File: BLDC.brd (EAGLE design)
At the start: 45.7 x 83.8 mm, 137 parts, among them U1 MCP2562, U2 STM32F405RGT6, U3 LM3671MF-3.3/NOPB, U4 DRV8302, Y1 8MHz

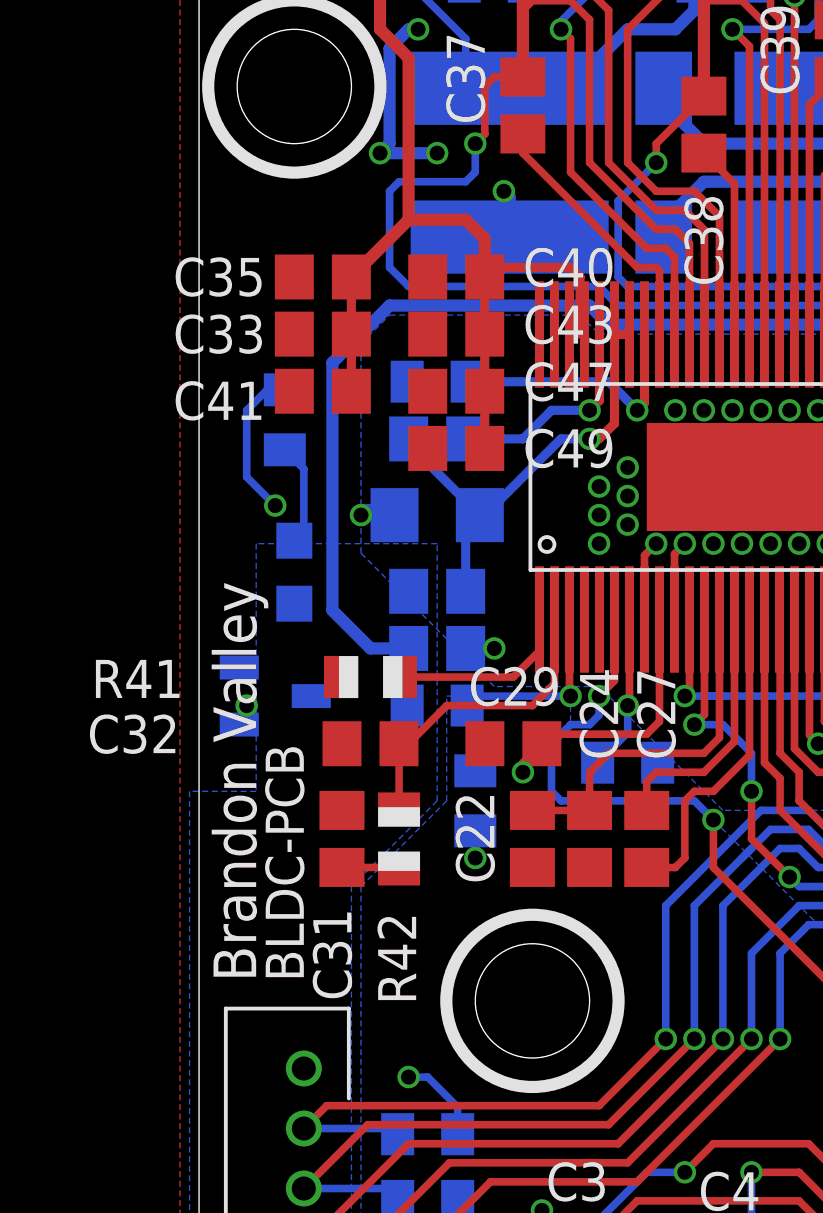
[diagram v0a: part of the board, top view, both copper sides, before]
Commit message: added big inductor and updated BOM a bit
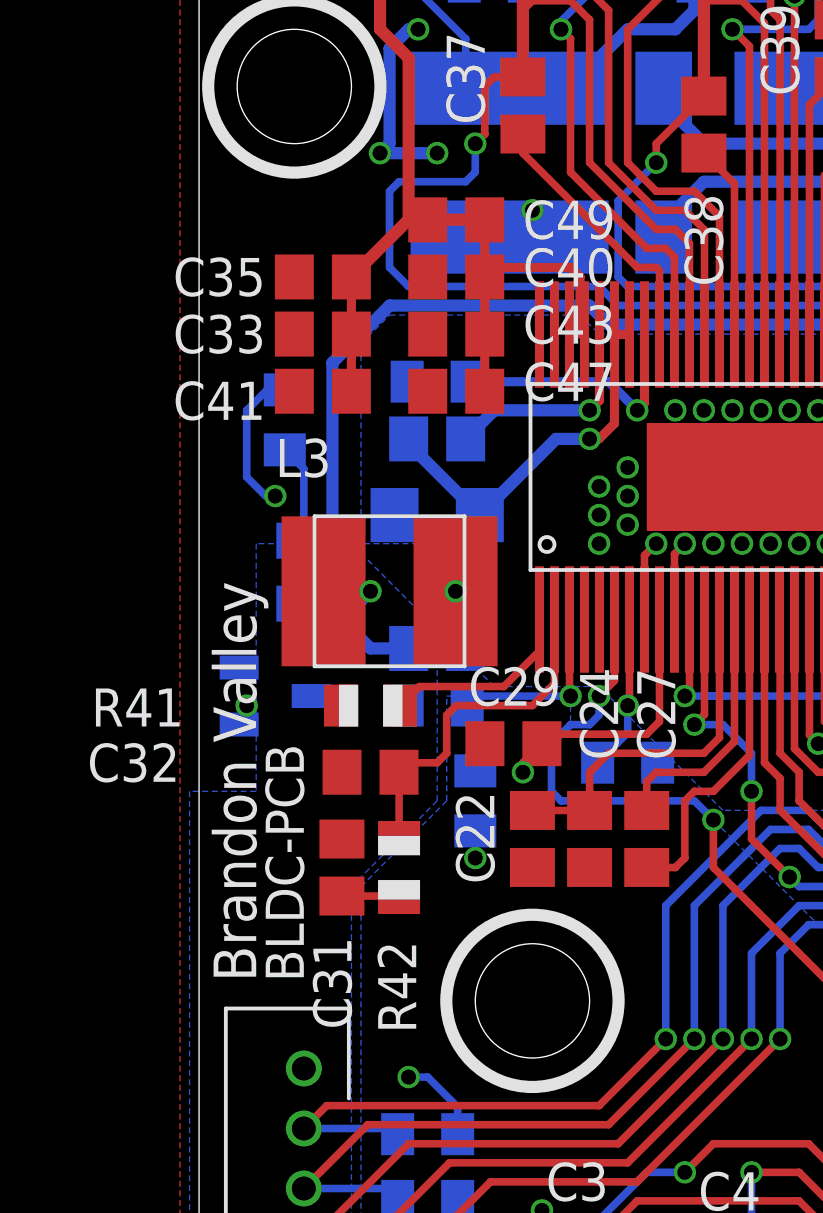
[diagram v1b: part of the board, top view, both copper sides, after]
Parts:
- removed L2: 22uH, FormE:0805
- added L3: 22uH, FormE:TYS5040220M-10
- C40: value 10uf, 50V -> 10uf,50V
- moved C49 7.62 mm to (8.57, 49.8)
- moved C31 0.95 mm to (4.76, 28.3)
- moved R41 0.95 mm to (5.71, 33.7)
- moved R42 0.95 mm to (6.67, 28.3)
- moved C32 0.95 mm to (5.71, 31.4)
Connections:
- net +5V: now also L3.P$2; no longer L2.2
- net N$21: now also L3.P$1; no longer L2.1
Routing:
- net +5V: track 103.1 -> 106.2 mm, vias 4 -> 5
- net GND: track 94.7 -> 91.9 mm, vias 76 -> 74
- net VCC: track 74.9 -> 72.7 mm
- net N$12: track 10.3 -> 11.8 mm
- net N$21: track 15.5 -> 16.6 mm, vias 1 -> 2

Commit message: added some large components at the last minute because I am a glutton for punishment
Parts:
- removed C33: 10uf,50V, rcl:C0805
- removed C44: 100n, rcl:C0805
- added C50: 10uf,50V, rcl:C1206
- added C51: 15uf,100V, FormE:K-55
- C34, C35, C36, C40, C42: device rcl:C0805 -> rcl:C1206
- C41: value 15uf,100V -> 10uf,50V; device rcl:C0805 -> rcl:C1206
- C43: value 10uf,50V -> 15uf,100V; device rcl:C0805 -> FormE:K-55
- C45: value 2.2n -> 100n
- C47: value 10uf,50V -> 2.2n
- C48: value 100uf -> 10uf,50V; device rcl:C0805 -> rcl:C1206
- C49: value 15uf,100V -> 100uf
- moved C45 26.4 mm to (10.2, 42.5), turned to 0 degrees
- moved C47 25.6 mm to (33.0, 51.8), flipped to the bottom, turned to 270 degrees
- moved C49 14.3 mm to (7.94, 35.6), flipped to the bottom
- moved C48 8.13 mm to (2.86, 41.9), turned to 0 degrees
- moved C43 7.63 mm to (3.17, 51.4), flipped to the bottom, turned to 90 degrees
- moved C40 7.38 mm to (1.91, 51.1), turned to 90 degrees
- moved C34 6.63 mm to (29.5, 51.8), turned to 270 degrees
- moved R53 5.93 mm to (9.84, 57.5)
- moved R30 5.32 mm to (1.27, 38.1)
- moved C42 4.97 mm to (27.0, 46.7)
- moved D2 3.31 mm to (11.1, 39.1), turned to 270 degrees
- moved C35 3.19 mm to (4.45, 51.1), turned to 90 degrees
- moved R43 2.22 mm to (10.2, 44.5)
- moved C41 2.03 mm to (2.86, 45.7), flipped to the bottom, turned to 0 degrees
- moved R51 1.91 mm to (9.84, 59.7)
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- renumbered L3 to L2
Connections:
- net +5V: now also C49.1; no longer C48.1
- net GND: now also C50.2, C51.2; no longer C33.2, C47.2
- net N$20: now also C45.1; no longer C44.1
- net N$21: now also C45.2; no longer C44.2
- net N$24: now also C46.1; no longer C45.1
- net N$26: now also C46.2; no longer C45.2
- net N$28: now also C47.2; no longer C46.2
- net N$29: now also C47.1; no longer C46.1
- net VCC: now also C48.1, C50.1, C51.1; no longer C33.1, C47.1, C49.1
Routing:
- net VCC: track 72.7 -> 81.6 mm, vias 0 -> 1
- net GND: track 91.9 -> 100.2 mm, vias 74 -> 77
- net N$24: track 22.6 -> 27.6 mm
- net H1_LOW: track 40.4 -> 35.7 mm
- net N$29: track 17.0 -> 20.2 mm
- net N$33: track 9.75 -> 6.65 mm
- net N$28: track 17.1 -> 19.7 mm
- net N$22: track 8.69 -> 6.47 mm
- net N$20: track 7.19 -> 4.97 mm
- net M_L1: track 16.2 -> 17.6 mm
- net N$21: track 16.6 -> 15.2 mm
- net ADC_TEMP: track 57.4 -> 56.2 mm
- net H3_VS: track 57.2 -> 58.1 mm
- net M_L3: track 21.4 -> 22.1 mm
- net +5V: track 106.2 -> 106.8 mm
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
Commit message: updated BOM
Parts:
- removed C50: 10uf,50V, rcl:C1206
- removed C51: 15uf,100V, FormE:K-55
- added C33: 15uf,100V, FormE:K-55
- added C44: 100n, rcl:C0805
- C45: value 100n -> 2.2n
- C47: value 2.2n -> 10uf,50V; device rcl:C0805 -> rcl:C1206
- C48: value 10uf,50V -> 100uf; device rcl:C1206 -> rcl:C0805
- C49: value 100uf -> 10uf,50V; device rcl:C0805 -> rcl:C1206
- moved R2 32.6 mm to (-7.30, -10.5)
- moved C47 31.7 mm to (2.86, 41.9), turned to 0 degrees
- moved C45 26.4 mm to (34.9, 51.8), turned to 270 degrees
- moved C49 9.69 mm to (2.86, 43.8), turned to 0 degrees
- moved C48 8.13 mm to (7.94, 35.6), turned to 180 degrees
- moved C43 8.11 mm to (7.30, 44.5), flipped to the top, turned to 270 degrees
- moved C46 1.90 mm to (33.0, 51.8)
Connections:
- net +5V: now also C48.1, R2.2; no longer C49.1, R2.1
- net GND: now also C33.2, C47.2; no longer C50.2, C51.2
- net N$20: now also C44.1; no longer C45.1
- net N$21: now also C44.2; no longer C45.2
- net N$24: now also C45.1; no longer C46.1
- net N$26: now also C45.2; no longer C46.2
- net N$28: now also C46.2; no longer C47.2
- net N$29: now also C46.1; no longer C47.1
- net N$5: now also R2.1; no longer R2.2
- net VCC: now also C33.1, C47.1, C49.1; no longer C48.1, C50.1, C51.1
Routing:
- net N$5: track 5.68 -> 4.40 mm
- net +5V: track 106.8 -> 105.9 mm

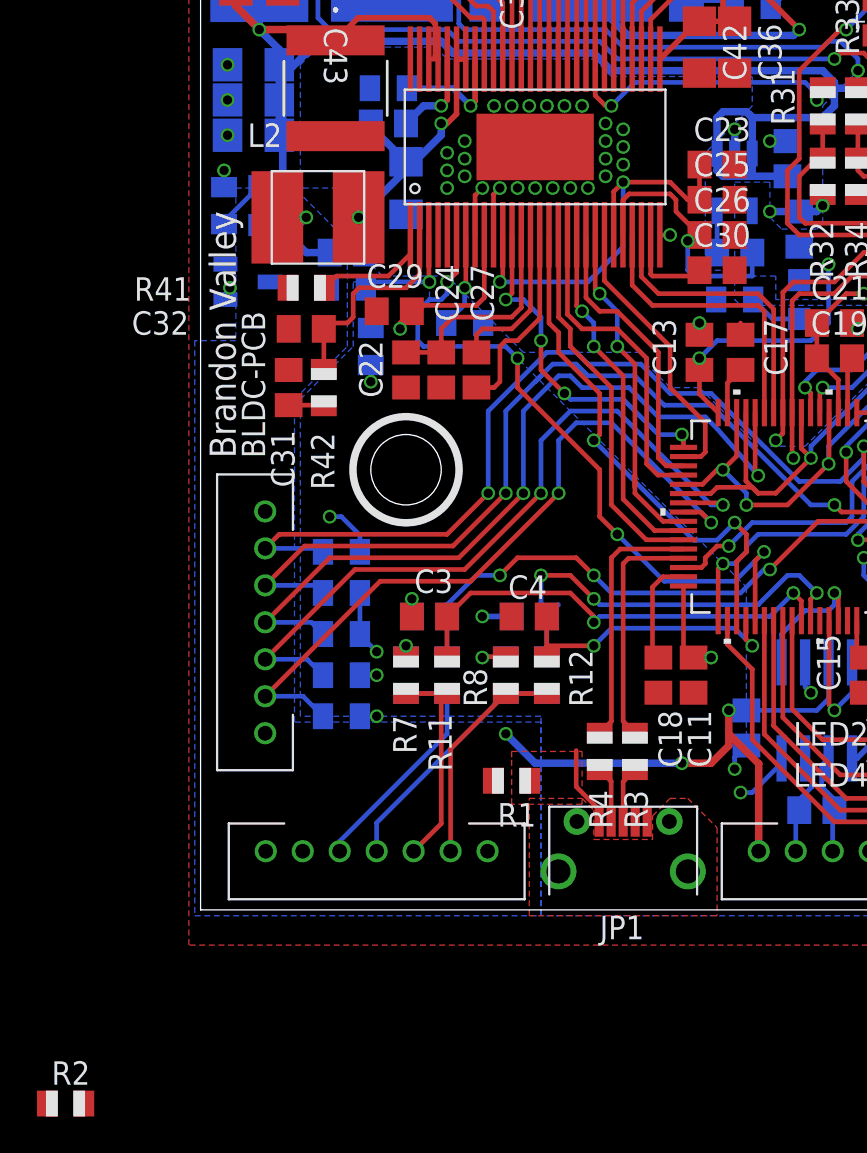
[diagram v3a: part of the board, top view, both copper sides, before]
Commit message: added jumper for DNP on usb
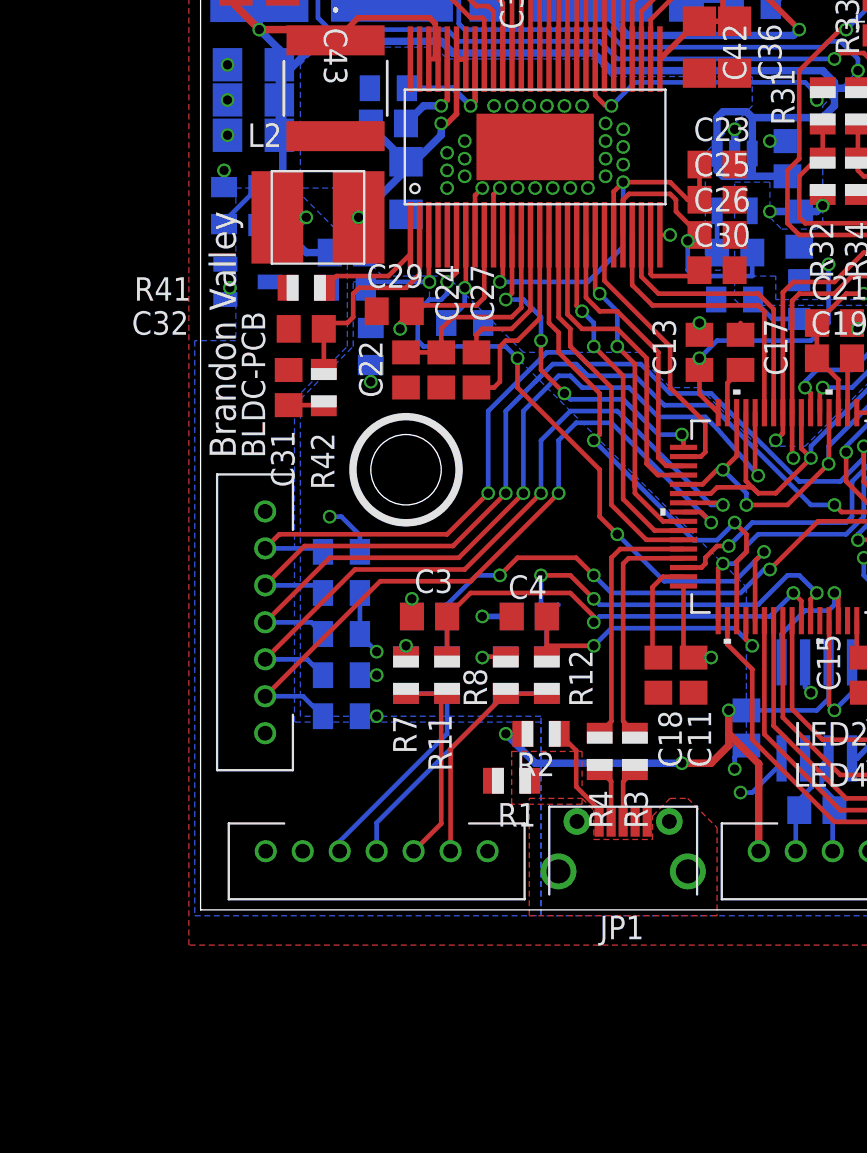
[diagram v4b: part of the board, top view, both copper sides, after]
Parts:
- moved R2 32.6 mm to (18.4, 9.53), turned to 180 degrees
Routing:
- net N$5: track 4.40 -> 5.68 mm
- net +5V: track 105.9 -> 106.6 mm
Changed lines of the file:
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@@
 <attribute name="PARTNO" value="KCM55WR72A156MH01K" x="7.3025" y="44.45" size="1.778" layer="27" rot="R270" display="off"/>
 </element>
-<element name="R2" library="adafruit" package="R0805" value="DNP" x="-7.3025" y="-10.4775">
-<attribute name="PARTNO" value="ERJ-6GEY0R00V" x="-7.3025" y="-10.4775" size="1.4224" layer="27" display="off"/>
+<element name="R2" library="adafruit" package="R0805" value="DNP" x="18.415" y="9.525" rot="R180">
+<attribute name="PARTNO" value="ERJ-6GEY0R00V" x="18.415" y="9.525" size="1.4224" layer="27" rot="R180" display="off"/>
 </element>
 </elements>
@@
 <wire x1="27.6225" y1="7.9375" x2="28.575" y2="8.89" width="0.4064" layer="1"/>
 <wire x1="28.575" y1="8.89" x2="28.575" y2="9.525" width="0.4064" layer="1"/>
-<wire x1="29.68625" y1="43.02125" x2="29.845" y2="42.8625" width="0.4064" layer="16"/>
 <wire x1="29.68625" y1="43.02125" x2="29.5275" y2="43.18" width="0.4064" layer="16"/>
 <wire x1="29.5275" y1="43.18" x2="28.2575" y2="43.18" width="0.4064" layer="16"/>
@@
 <wire x1="34.29" y1="43.4975" x2="33.655" y2="42.8625" width="0.4064" layer="16"/>
 <contactref element="R2" pad="2"/>
-<wire x1="5.525" y1="3.175" x2="-6.3025" y2="-10.4775" width="0" layer="19" extent="1-1"/>
+<wire x1="17.415" y1="9.525" x2="16.51" y2="9.525" width="0.254" layer="1"/>
 </signal>
 <signal name="+3V3">
@@
 <wire x1="21.56" y1="4.7578" x2="21.59" y2="4.7878" width="0.254" layer="1"/>
 <wire x1="21.59" y1="4.7878" x2="21.59" y2="5.3975" width="0.254" layer="1"/>
-<wire x1="20.32" y1="6.6675" x2="20.32" y2="8.62" width="0.254" layer="1"/>
+<wire x1="20.32" y1="8.62" x2="20.32" y2="6.6675" width="0.254" layer="1"/>
 <wire x1="21.59" y1="5.3975" x2="20.32" y2="6.6675" width="0.254" layer="1"/>
 <contactref element="R2" pad="1"/>
-<wire x1="-8.3025" y1="-10.4775" x2="20.32" y2="6.6675" width="0" layer="19" extent="1-1"/>
+<wire x1="19.415" y1="9.525" x2="20.32" y2="8.62" width="0.254" layer="1"/>
 </signal>
 <signal name="N$3">

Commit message: fixed brd errors
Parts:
- moved C20 0.71 mm to (32.4, 41.0)
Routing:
- net N$24: track 27.6 -> 28.8 mm
- net +5V: track 106.6 -> 106.0 mm
- net GND: track 100.2 -> 100.0 mm, vias 77 -> 76
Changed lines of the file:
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@@
 <attribute name="VALUE" x="39.37" y="19.3675" size="1.27" layer="28" rot="MR0"/>
 </element>
-<element name="C20" library="rcl" package="C0805" value="4.7uF" x="31.75" y="40.64" smashed="yes" rot="MR90">
-<attribute name="PARTNO" value="GRM21BC81E475KA12L" x="31.75" y="40.64" size="1.778" layer="28" rot="MR90" display="off"/>
-<attribute name="NAME" x="33.02" y="39.37" size="1.27" layer="26" rot="MR90"/>
-<attribute name="VALUE" x="29.21" y="39.37" size="1.27" layer="28" rot="MR90"/>
+<element name="C20" library="rcl" package="C0805" value="4.7uF" x="32.385" y="40.9575" smashed="yes" rot="MR90">
+<attribute name="PARTNO" value="GRM21BC81E475KA12L" x="32.385" y="40.9575" size="1.778" layer="28" rot="MR90" display="off"/>
+<attribute name="NAME" x="33.655" y="39.6875" size="1.27" layer="26" rot="MR90"/>
+<attribute name="VALUE" x="29.845" y="39.6875" size="1.27" layer="28" rot="MR90"/>
 </element>
 <element name="C8" library="rcl" package="C0805" value="15p" x="38.1" y="16.8275" smashed="yes" rot="MR0">
@@
 <vertex x="21.2725" y="46.0375"/>
 <vertex x="22.225" y="45.085"/>
-<vertex x="29.845" y="45.085"/>
-<vertex x="29.845" y="43.4975"/>
-<vertex x="27.305" y="40.9575"/>
+<vertex x="33.9725" y="45.085"/>
+<vertex x="33.9725" y="40.3225"/>
+<vertex x="27.305" y="40.3225"/>
 <vertex x="27.305" y="34.6075"/>
 <vertex x="28.8925" y="34.6075"/>
@@
 <wire x1="28.8925" y1="40.92" x2="28.8925" y2="42.2275" width="0.4064" layer="16"/>
 <via x="28.8925" y="42.2275" extent="1-16" drill="0.5"/>
-<wire x1="31.75" y1="41.59" x2="31.7475" y2="41.5925" width="0.254" layer="16"/>
 <wire x1="32.385" y1="37.78" x2="30.8" y2="37.78" width="0.4064" layer="16"/>
 <wire x1="30.8" y1="37.78" x2="30.7975" y2="37.7825" width="0.4064" layer="16"/>
 <via x="30.7975" y="37.7825" extent="1-16" drill="0.5"/>
-<wire x1="31.7475" y1="41.5925" x2="30.7975" y2="41.5925" width="0.4064" layer="16"/>
-<via x="30.7975" y="41.5925" extent="1-16" drill="0.5"/>
 <wire x1="33.655" y1="38.6875" x2="33.655" y2="38.1" width="0.4064" layer="1"/>
 <via x="33.655" y="38.1" extent="1-16" drill="0.5"/>
@@
 <contactref element="C14" pad="2"/>
 <contactref element="C21" pad="2"/>
-<wire x1="10.3525" y1="49.2725" x2="11.1125" y2="50.0325" width="0.254" layer="16"/>
-<wire x1="11.1125" y1="50.0325" x2="11.1125" y2="50.165" width="0.254" layer="16"/>
-<via x="11.1125" y="50.165" extent="1-16" drill="0.5"/>
+<via x="10.16" y="51.1175" extent="1-16" drill="0.5"/>
 <contactref element="C35" pad="2"/>
 <contactref element="C40" pad="2"/>
@@
 <via x="1.4575" y="43.815" extent="1-16" drill="0.5"/>
 <via x="1.4575" y="45.72" extent="1-16" drill="0.5"/>
+<wire x1="10.16" y1="51.1175" x2="10.3525" y2="50.925" width="0.4064" layer="16"/>
+<wire x1="10.3525" y1="50.925" x2="10.3525" y2="49.2725" width="0.4064" layer="16"/>
 </signal>
 <signal name="+5V">
@@
 <wire x1="27.6225" y1="7.9375" x2="28.575" y2="8.89" width="0.4064" layer="1"/>
 <wire x1="28.575" y1="8.89" x2="28.575" y2="9.525" width="0.4064" layer="1"/>
-<wire x1="29.68625" y1="43.02125" x2="29.5275" y2="43.18" width="0.4064" layer="16"/>
 <wire x1="29.5275" y1="43.18" x2="28.2575" y2="43.18" width="0.4064" layer="16"/>
 <wire x1="28.2575" y1="43.18" x2="27.94" y2="42.8625" width="0.4064" layer="16"/>
@@
 <wire x1="18.0975" y1="7.9375" x2="16.51" y2="9.525" width="0.4064" layer="16"/>
 <wire x1="26.035" y1="7.9375" x2="18.0975" y2="7.9375" width="0.4064" layer="16"/>
-<wire x1="4.445" y1="45.085" x2="6.35" y2="46.99" width="0.4064" layer="16"/>
 <contactref element="LED5" pad="A"/>
 <wire x1="5.715" y1="35.56" x2="4.445" y2="36.83" width="0.4064" layer="16"/>
-<wire x1="4.445" y1="36.83" x2="4.445" y2="45.085" width="0.4064" layer="16"/>
 <contactref element="L2" pad="P$2"/>
 <wire x1="4.445" y1="36.83" x2="5.08" y2="36.83" width="0.4064" layer="16"/>
-<wire x1="5.08" y1="36.83" x2="5.715" y2="37.465" width="0.4064" layer="16"/>
+<wire x1="5.715" y1="37.465" x2="5.08" y2="36.83" width="0.4064" layer="16"/>
 <via x="5.715" y="37.465" extent="1-16" drill="0.5"/>
 <wire x1="5.715" y1="37.465" x2="4.15" y2="37.465" width="0.4064" layer="1"/>
 <wire x1="34.29" y1="44.7675" x2="34.29" y2="44.45" width="0.4064" layer="16"/>
-<wire x1="31.75" y1="39.69" x2="29.2125" y2="39.69" width="0.4064" layer="16"/>
 <wire x1="29.2125" y1="39.69" x2="29.21" y2="39.6875" width="0.4064" layer="16"/>
-<wire x1="34.29" y1="44.45" x2="34.29" y2="43.4975" width="0.4064" layer="16"/>
-<wire x1="33.655" y1="42.8625" x2="29.845" y2="42.8625" width="0.4064" layer="16"/>
-<wire x1="29.845" y1="42.8625" x2="29.68625" y2="43.02125" width="0.4064" layer="16"/>
-<wire x1="34.29" y1="43.4975" x2="33.655" y2="42.8625" width="0.4064" layer="16"/>
+<wire x1="29.845" y1="42.8625" x2="29.5275" y2="43.18" width="0.4064" layer="16"/>
 <contactref element="R2" pad="2"/>
 <wire x1="17.415" y1="9.525" x2="16.51" y2="9.525" width="0.254" layer="1"/>
+<wire x1="34.29" y1="40.9575" x2="33.3375" y2="40.005" width="0.4064" layer="16"/>
+<wire x1="33.3375" y1="40.005" x2="32.3875" y2="40.005" width="0.4064" layer="16"/>
+<wire x1="32.385" y1="40.0075" x2="32.3875" y2="40.005" width="0.4064" layer="16"/>
+<wire x1="34.29" y1="44.45" x2="34.29" y2="40.9575" width="0.4064" layer="16"/>
+<wire x1="29.5275" y1="39.6875" x2="32.065" y2="39.6875" width="0.4064" layer="16"/>
+<wire x1="32.065" y1="39.6875" x2="32.385" y2="40.0075" width="0.4064" layer="16"/>
+<wire x1="6.35" y1="46.99" x2="5.715" y2="46.355" width="0.4064" layer="16"/>
+<wire x1="5.715" y1="46.355" x2="5.715" y2="37.465" width="0.4064" layer="16"/>
 </signal>
 <signal name="+3V3">
@@
 <wire x1="22.8475" y1="49.5175" x2="25.7175" y2="52.3875" width="0.254" layer="1"/>
 <wire x1="34.925" y1="52.7025" x2="34.925" y2="53.0225" width="0.4064" layer="16"/>
-<via x="33.3375" y="55.5625" extent="1-16" drill="0.5"/>
+<via x="33.9725" y="55.5625" extent="1-16" drill="0.5"/>
 <wire x1="30.845" y1="54.6575" x2="30.845" y2="54.61" width="0.254" layer="16"/>
 <wire x1="30.845" y1="54.61" x2="30.845" y2="54.975" width="0.254" layer="16"/>
 <wire x1="30.845" y1="54.975" x2="31.4325" y2="55.5625" width="0.254" layer="16"/>
-<wire x1="31.4325" y1="55.5625" x2="33.3375" y2="55.5625" width="0.254" layer="16"/>
+<wire x1="31.4325" y1="55.5625" x2="33.9725" y2="55.5625" width="0.254" layer="16"/>
 <wire x1="33.02" y1="54.61" x2="34.925" y2="52.705" width="0.4064" layer="16"/>
 <wire x1="34.925" y1="52.705" x2="34.925" y2="52.7025" width="0.4064" layer="16"/>
@@
 <wire x1="25.7175" y1="52.3875" x2="25.7175" y2="55.245" width="0.254" layer="1"/>
 <wire x1="25.7175" y1="55.245" x2="27.305" y2="56.8325" width="0.254" layer="1"/>
-<wire x1="32.0675" y1="56.8325" x2="33.3375" y2="55.5625" width="0.254" layer="1"/>
-<wire x1="27.305" y1="56.8325" x2="32.0675" y2="56.8325" width="0.254" layer="1"/>
+<wire x1="32.7025" y1="56.8325" x2="33.9725" y2="55.5625" width="0.254" layer="1"/>
+<wire x1="27.305" y1="56.8325" x2="32.7025" y2="56.8325" width="0.254" layer="1"/>
 </signal>
 <signal name="N$26">

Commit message: made brd look all pretty
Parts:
- moved R43 0.63 mm to (10.2, 45.1)
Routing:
- net GND: track 100.0 -> 104.1 mm, vias 76 -> 75
- net H1_LOW: track 35.7 -> 37.7 mm
- net H1_VS: track 79.0 -> 77.7 mm
- net M_L1: track 17.6 -> 17.1 mm
- net DC_CAL: track 18.6 -> 18.0 mm
